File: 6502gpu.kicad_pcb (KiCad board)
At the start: 4 copper layers, 140 x 110 mm, 102 parts, among them J1 Conn_01x02, J10 Conn_01x10, J11 Conn_01x03, J12 Conn_01x03, J13 Conn_01x03, J14 Conn_01x03, J15 Conn_01x03, J16 Conn_01x01, J17 Barrel_Jack, J2 Conn_01x08, J3 Conn_01x02, J4 Conn_01x16, J5 Conn_01x02, J6 Conn_01x03, J7 DE15_Receptacle_HighDensity, J8 Conn_01x08, J9 Conn_01x10, U1 74HC86, U10 74AHC30, U11 74AHC30, U12 74AHC30, U13 74AHC30, U14 74LV163, U15 74LV04, U16 74AC109, U17 74LV163, U18 74LV04, U19 74LV08, U2 74HC00, U20 74LV163, U21 74AHC30, U22 74AHC30, U23 74AHC30, U24 74AHC30, U25 74AC109, U26 74LV163, U27 74LV163, U28 74LV163, U29 74HC377, U3 74LV27, U30 74LV32, U31 74LV32, U32 74LV08, U33 74LV08, U34 LM7805, U4 74HC00, U5 74CBT16390, U6 74CBT16390, U7 AS7C256A-10, U8 AS7C256A-10, U9 74CBT16390, X1 25.175MHz

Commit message: Done routing!!
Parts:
- removed J17: Barrel_Jack, Connector_BarrelJack:BarrelJack_CUI_PJ-102AH_Horizontal
- removed U34: LM7805, Package_TO_SOT_THT:TO-220-3_Vertical
- moved C3 100.6 mm to (184.2, 127.0), turned to 90 degrees
- moved U3 96.9 mm to (176.5, 127.0), turned to 90 degrees
- moved C4 53.7 mm to (118.1, 125.7), turned to -90 degrees
- moved U4 14.0 mm to (111.8, 125.7)
- moved C35 6.75 mm to (183.5, 135.3), turned to -90 degrees
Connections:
- U1 pad 10: Net-(U1-Pad10) -> GND
- U1 pad 11: unconnected-(U1-Pad11) -> /~{WriteReg}
- U1 pad 12: GND -> +5V
- U1 pad 13: GND -> Net-(U1-Pad13)
- U1 pad 8: /~{WriteReg} -> unconnected-(U1-Pad8)
- U1 pad 9: +5V -> GND
- U29 pad 2: /ConfigReg/BufSel -> /Memory/BufSel
- U3 pad 10: /~{FbSel} -> /R~{W}
- U3 pad 11: /R~{W} -> /~{Phi2}
- U3 pad 3: /~{Phi2} -> /~{RegSel}
- U3 pad 6: /WriteMem -> Net-(U1-Pad13)
- U3 pad 8: Net-(U1-Pad10) -> /WriteMem
- U3 pad 9: /~{RegSel} -> /~{FbSel}
- U4 pad 1: /ConfigReg/BufSel -> /Memory/BufSel
- U4 pad 10: /WriteMem -> GND
- U4 pad 11: unconnected-(U4-Pad11) -> /Memory/~{WeB}
- U4 pad 12: GND -> /Memory/BufSel
- U4 pad 13: GND -> /WriteMem
- U4 pad 2: /ConfigReg/BufSel -> /Memory/BufSel
- U4 pad 8: /Memory/~{WeB} -> unconnected-(U4-Pad8)
- U4 pad 9: /ConfigReg/BufSel -> GND
- U5 pad 30: /ConfigReg/BufSel -> /Memory/BufSel
- U6 pad 30: /ConfigReg/BufSel -> /Memory/BufSel
- U8 pad 22: /ConfigReg/BufSel -> /Memory/BufSel
- U9 pad 30: /ConfigReg/BufSel -> /Memory/BufSel
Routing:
- net /Memory/BufSel: track 0.00 -> 129.6 mm, vias 0 -> 5
- net /WriteMem: track 0.00 -> 99.3 mm, vias 0 -> 2
- net /~{Phi2}: track 0.00 -> 91.0 mm, vias 0 -> 2
- net /DAC/~{BlankBlack}: track 66.2 -> 152.0 mm
- net /~{WriteReg}: track 0.00 -> 77.5 mm
- net /ConfigReg/BufSel: track 68.6 -> 0.00 mm, vias 3 -> 0
- net /Memory/~{WeB}: track 0.00 -> 66.2 mm, vias 0 -> 2
- net /HBlank: track 126.5 -> 74.7 mm, vias 3 -> 0
- net /Memory/AddrCPU14: track 18.9 -> 69.8 mm, vias 1 -> 4
- net /ConfigReg/NmiEnable: track 0.00 -> 48.5 mm
- net /ConfigReg/BlankBlack: track 46.6 -> 93.3 mm, vias 0 -> 2
- net /~{RegSel}: track 0.73 -> 42.9 mm
- net /Memory/~{WeA}: track 0.00 -> 41.6 mm, vias 0 -> 2
- net /Memory/~{BufSel}: track 96.1 -> 129.9 mm, vias 3 -> 5
- net Net-(U1-Pad13): track 0.00 -> 28.6 mm, vias 0 -> 2
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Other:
- board text added: "Adapter Specs: 64KB VRAM, split into 2 buffers"

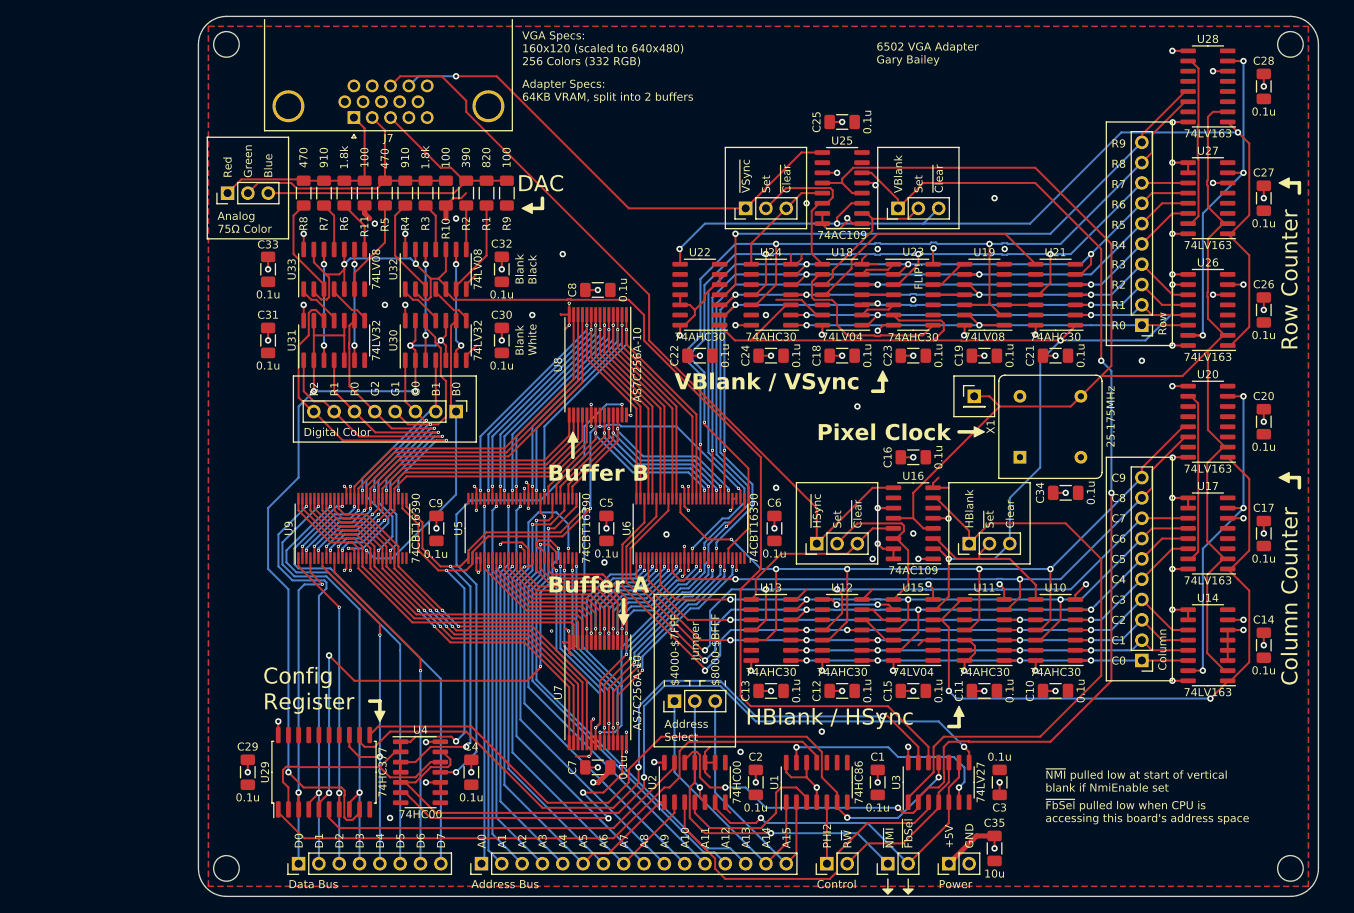
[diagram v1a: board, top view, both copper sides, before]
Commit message: Make DRC quiet, add loooots of vias
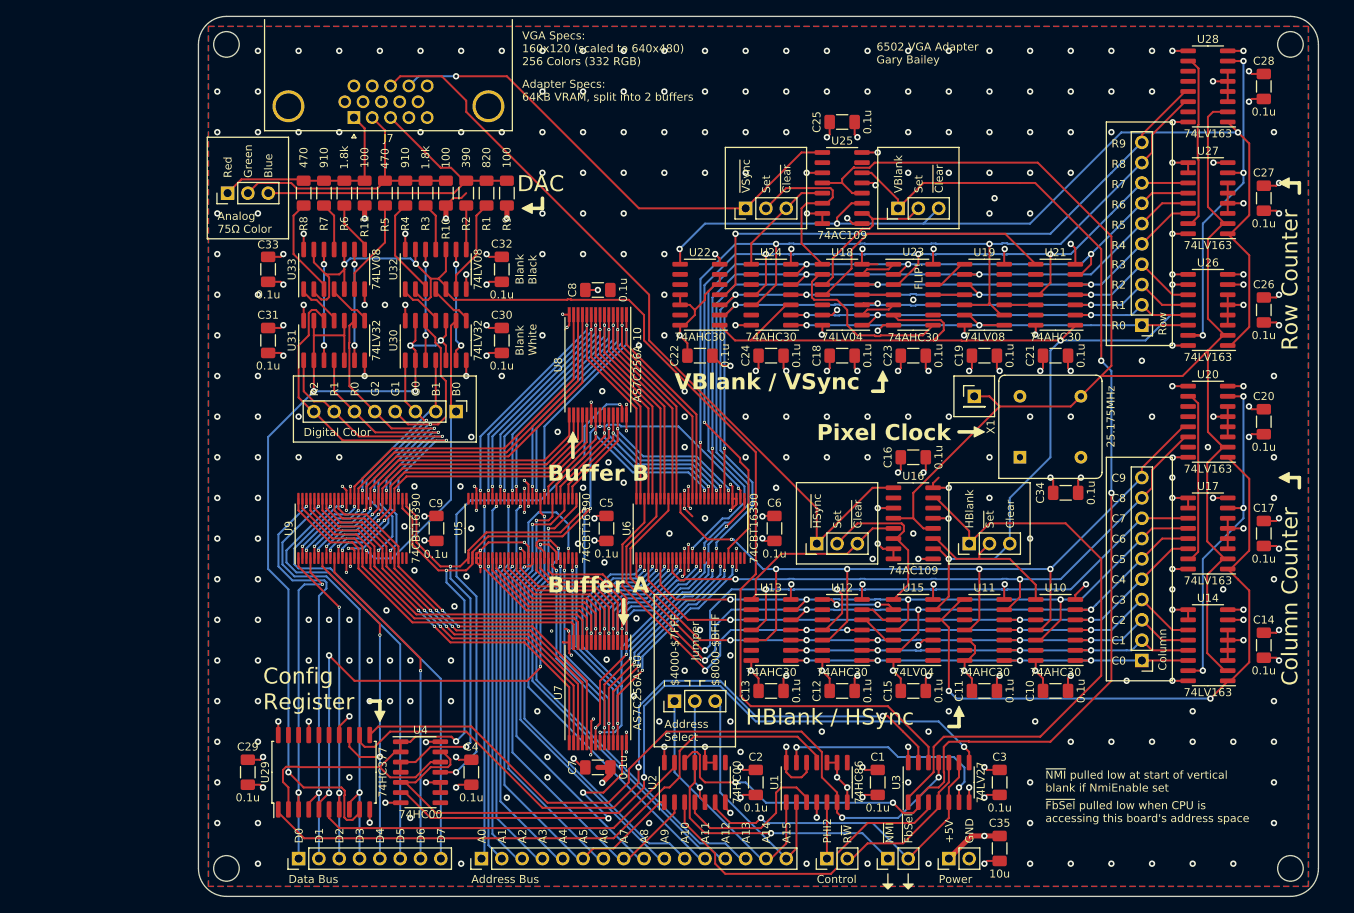
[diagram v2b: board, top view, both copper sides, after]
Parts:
- J7: footprint Connector_Dsub:DSUB-15-HD_Female_Horizontal_P2.29x1.98mm_EdgePinOffset8.35mm_Housed_MountingHolesOffset10.89mm -> custom:DSUB-15-HD_Female_Horizontal_P2.29x1.98mm_EdgePinOffset8.35mm_Housed_MountingHolesOffset10.89mm
- moved C35 0.64 mm to (184.2, 135.3)
- moved J1 0.63 mm to (162.6, 136.5)
- moved J2 0.63 mm to (96.5, 136.5)
- moved J3 0.63 mm to (177.8, 136.5)
- moved J4 0.63 mm to (119.4, 136.5)
- moved J5 0.63 mm to (170.2, 136.5)
- turned C3 to -90 degrees
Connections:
- U10 pad 10: (no net) -> unconnected-(U10B-NC-Pad10)
- U10 pad 13: (no net) -> unconnected-(U10B-NC-Pad13)
- U10 pad 9: (no net) -> unconnected-(U10B-NC-Pad9)
- U11 pad 10: (no net) -> unconnected-(U11B-NC-Pad10)
- U11 pad 13: (no net) -> unconnected-(U11B-NC-Pad13)
- U11 pad 9: (no net) -> unconnected-(U11B-NC-Pad9)
- U12 pad 10: (no net) -> unconnected-(U12B-NC-Pad10)
- U12 pad 13: (no net) -> unconnected-(U12B-NC-Pad13)
- U12 pad 9: (no net) -> unconnected-(U12B-NC-Pad9)
- U13 pad 10: (no net) -> unconnected-(U13B-NC-Pad10)
- U13 pad 13: (no net) -> unconnected-(U13B-NC-Pad13)
- U13 pad 9: (no net) -> unconnected-(U13B-NC-Pad9)
- U21 pad 10: (no net) -> unconnected-(U21B-NC-Pad10)
- U21 pad 13: (no net) -> unconnected-(U21B-NC-Pad13)
- U21 pad 9: (no net) -> unconnected-(U21B-NC-Pad9)
- U22 pad 10: (no net) -> unconnected-(U22B-NC-Pad10)
- U22 pad 13: (no net) -> unconnected-(U22B-NC-Pad13)
- U22 pad 9: (no net) -> unconnected-(U22B-NC-Pad9)
- U23 pad 10: (no net) -> unconnected-(U23B-NC-Pad10)
- U23 pad 13: (no net) -> unconnected-(U23B-NC-Pad13)
- U23 pad 9: (no net) -> unconnected-(U23B-NC-Pad9)
- U24 pad 10: (no net) -> unconnected-(U24B-NC-Pad10)
- U24 pad 13: (no net) -> unconnected-(U24B-NC-Pad13)
- U24 pad 9: (no net) -> unconnected-(U24B-NC-Pad9)
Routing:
- net GND: track 127.3 -> 267.8 mm, vias 54 -> 334
- net +5V: track 182.8 -> 206.9 mm
- net /Counters/VSyncSet: track 20.9 -> 22.9 mm
- net /Counters/Row8: track 122.8 -> 121.4 mm
- net /AddrPhys15: track 32.2 -> 30.9 mm
- net /Counters/Row7: track 122.2 -> 121.0 mm
- net /~{RegSel}: track 42.9 -> 41.7 mm
- net /~{Phi2}: track 91.0 -> 91.9 mm
- net /~{FbSel}: track 43.5 -> 42.6 mm
- net /Memory/AddrCPU10: track 56.2 -> 57.1 mm
- net Net-(U18-Pad11): track 32.0 -> 32.8 mm
- net /Memory/AddrCPU1: track 38.9 -> 38.3 mm
- net /ConfigReg/DataIn5: track 56.1 -> 55.5 mm
- net /ConfigReg/DataIn1: track 54.9 -> 54.2 mm
- net /Phi2: track 7.69 -> 7.05 mm
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
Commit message: Test exporting
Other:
- board text added: "JLCJLCJLCJLC"
